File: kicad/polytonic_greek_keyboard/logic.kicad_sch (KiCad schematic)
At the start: 1 part, among them U1 ESP32-S2-WROVER

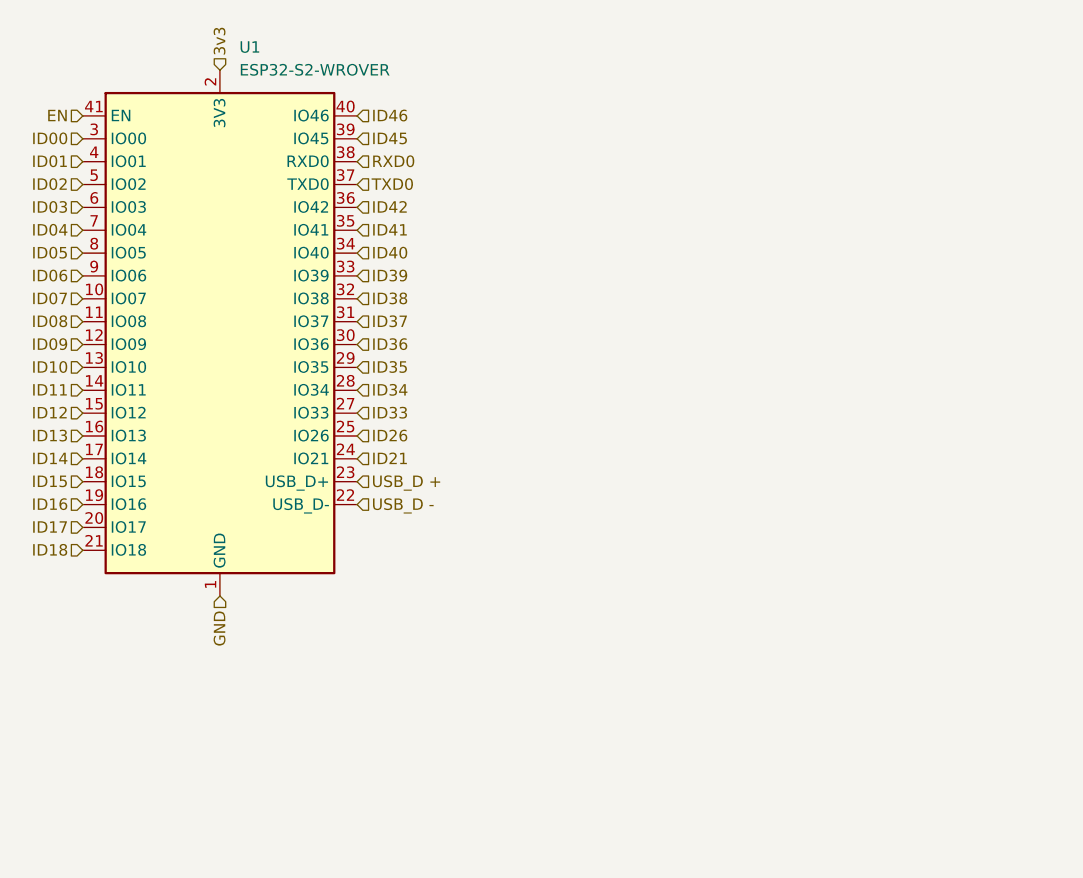
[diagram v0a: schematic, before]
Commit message: [UPDATE] the board desing, [FIX] connection issues
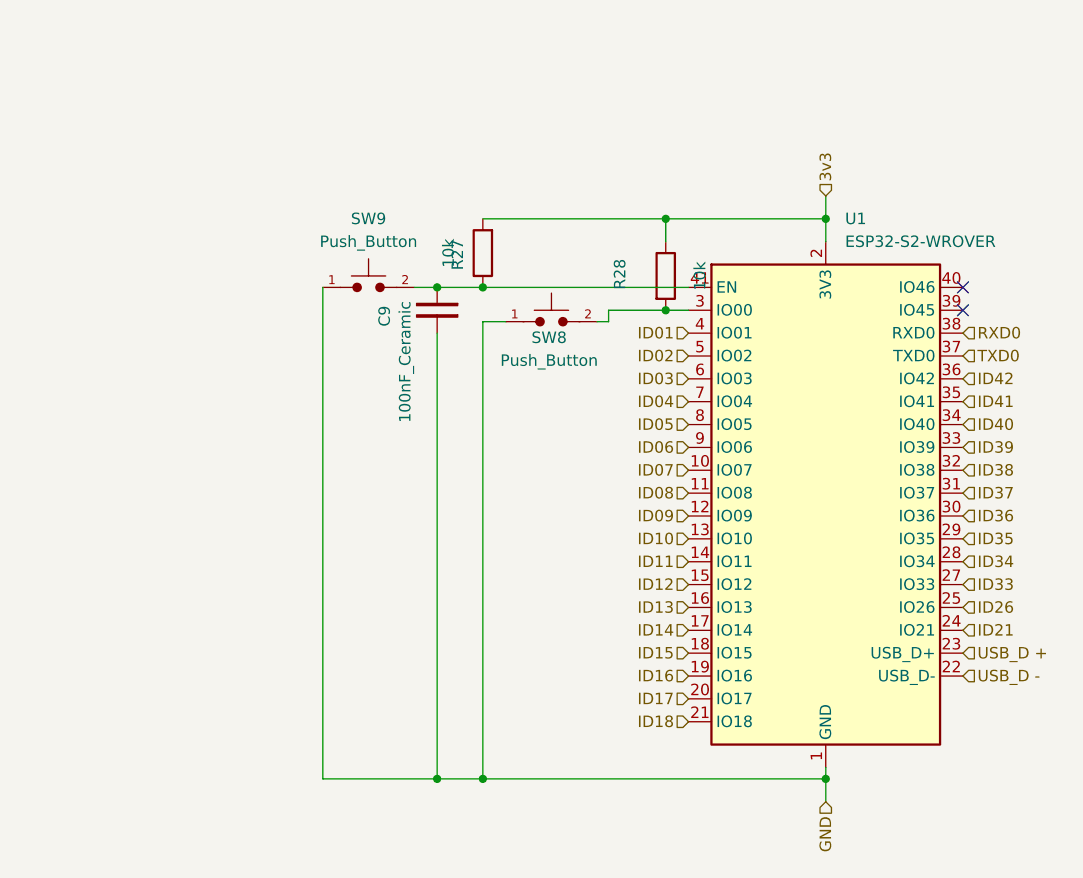
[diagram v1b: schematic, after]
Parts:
- added C9: 100nF_Ceramic, Capacitor_THT:C_Disc_D5.0mm_W2.5mm_P2.50mm, symbol PCM_SL_Capacitors:100nF_Ceramic
- added R27, R28: 10k_0402, Resistor_SMD:R_0402_1005Metric, symbol PCM_4ms_Resistor:10k_0402
- added SW8, SW9: Push_Button, Button_Switch_THT:SW_PUSH_6mm, symbol PCM_SL_Devices:Push_Button
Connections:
- net 3v3: now also R27.2, R28.1
- net GND: now also C9.2, SW8.1, SW9.1
- net EN: no longer names the net of U1.41 (EN)
- net EN: now also C9.1, R27.1, SW9.2
- net ID00: no longer names the net of U1.3 (IO00)
- net ID00: now also R28.2, SW8.2
- net ID45: no longer names the net of U1.39 (IO45)
- net ID46: no longer names the net of U1.40 (IO46)
- no-connect marks 0 -> 2
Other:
- moved on the sheet: U1

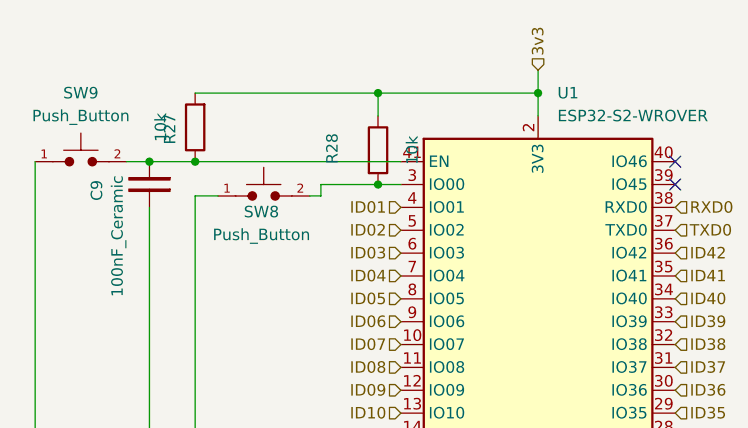
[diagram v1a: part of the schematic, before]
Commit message: [UPDATE] the desing to fit on two separate pcbs
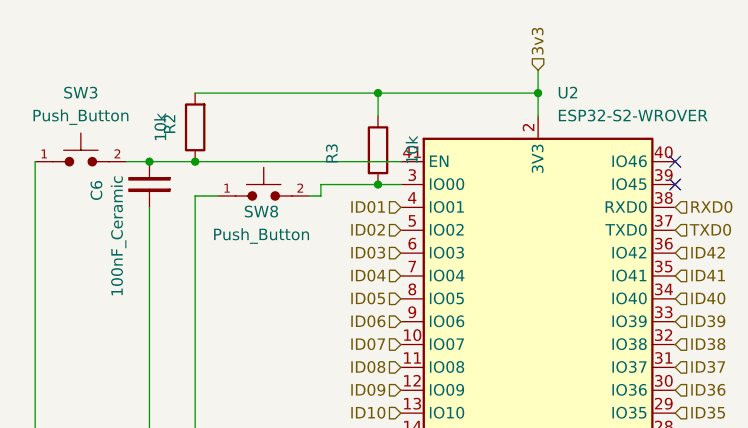
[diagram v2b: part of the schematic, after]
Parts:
- renumbered C9 to C6, R27 to R2, R28 to R3, SW9 to SW3, U1 to U2
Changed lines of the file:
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@@
 		(on_board yes)
 		(dnp no)
-		(property "Reference" "R28"
+		(property "Reference" "R3"
 			(at 90.17 47.244 90)
 			(effects
@@
 		(instances
 			(project "polytonic_greek_keyboard"
-				(path "/cbe25a1b-6c02-43c2-9ff9-ba274c7cf6a2/98a216ce-7319-4f0b-a321-c8ded0ff5837"
-					(reference "R28")
+				(path "/cbe25a1b-6c02-43c2-9ff9-ba274c7cf6a2/8498b325-11fd-4b20-a704-75ec3d8987ef/52990bdd-0b84-441a-b927-02579db6fb17"
+					(reference "R3")
 					(unit 1)
 				)
@@
 		(dnp no)
 		(fields_autoplaced yes)
-		(property "Reference" "U1"
+		(property "Reference" "U2"
 			(at 115.1733 39.37 0)
 			(effects
@@
 		)
 		(instances
-			(project ""
-				(path "/cbe25a1b-6c02-43c2-9ff9-ba274c7cf6a2/98a216ce-7319-4f0b-a321-c8ded0ff5837"
-					(reference "U1")
+			(project "polytonic_greek_keyboard"
+				(path "/cbe25a1b-6c02-43c2-9ff9-ba274c7cf6a2/8498b325-11fd-4b20-a704-75ec3d8987ef/52990bdd-0b84-441a-b927-02579db6fb17"
+					(reference "U2")
 					(unit 1)
 				)
@@
 		(on_board yes)
 		(dnp no)
-		(property "Reference" "C9"
+		(property "Reference" "C6"
 			(at 64.008 49.022 0)
 			(effects
@@
 		)
 		(instances
-			(project ""
-				(path "/cbe25a1b-6c02-43c2-9ff9-ba274c7cf6a2/98a216ce-7319-4f0b-a321-c8ded0ff5837"
-					(reference "C9")
+			(project "polytonic_greek_keyboard"
+				(path "/cbe25a1b-6c02-43c2-9ff9-ba274c7cf6a2/8498b325-11fd-4b20-a704-75ec3d8987ef/52990bdd-0b84-441a-b927-02579db6fb17"
+					(reference "C6")
 					(unit 1)
 				)
@@
 		(dnp no)
 		(fields_autoplaced yes)
-		(property "Reference" "SW9"
+		(property "Reference" "SW3"
 			(at 62.23 39.37 0)
 			(effects
@@
 		)
 		(instances
-			(project ""
-				(path "/cbe25a1b-6c02-43c2-9ff9-ba274c7cf6a2/98a216ce-7319-4f0b-a321-c8ded0ff5837"
-					(reference "SW9")
+			(project "polytonic_greek_keyboard"
+				(path "/cbe25a1b-6c02-43c2-9ff9-ba274c7cf6a2/8498b325-11fd-4b20-a704-75ec3d8987ef/52990bdd-0b84-441a-b927-02579db6fb17"
+					(reference "SW3")
 					(unit 1)
 				)
@@
 		(on_board yes)
 		(dnp no)
-		(property "Reference" "R27"
+		(property "Reference" "R2"
 			(at 72.136 41.656 90)
 			(effects
@@
 		)
 		(instances
-			(project ""
-				(path "/cbe25a1b-6c02-43c2-9ff9-ba274c7cf6a2/98a216ce-7319-4f0b-a321-c8ded0ff5837"
-					(reference "R27")
+			(project "polytonic_greek_keyboard"
+				(path "/cbe25a1b-6c02-43c2-9ff9-ba274c7cf6a2/8498b325-11fd-4b20-a704-75ec3d8987ef/52990bdd-0b84-441a-b927-02579db6fb17"
+					(reference "R2")
 					(unit 1)
 				)
@@
 		(instances
 			(project "polytonic_greek_keyboard"
-				(path "/cbe25a1b-6c02-43c2-9ff9-ba274c7cf6a2/98a216ce-7319-4f0b-a321-c8ded0ff5837"
+				(path "/cbe25a1b-6c02-43c2-9ff9-ba274c7cf6a2/8498b325-11fd-4b20-a704-75ec3d8987ef/52990bdd-0b84-441a-b927-02579db6fb17"
 					(reference "SW8")
 					(unit 1)

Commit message: [UPDATE] anotation issues
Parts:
- renumbered C6 to C4, R3 to R10, R2 to R9, SW8 to SW4, U2 to U3
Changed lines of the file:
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@@
 		(on_board yes)
 		(dnp no)
-		(property "Reference" "R3"
+		(property "Reference" "R10"
 			(at 90.17 47.244 90)
 			(effects
@@
 			(project "polytonic_greek_keyboard"
 				(path "/cbe25a1b-6c02-43c2-9ff9-ba274c7cf6a2/8498b325-11fd-4b20-a704-75ec3d8987ef/52990bdd-0b84-441a-b927-02579db6fb17"
-					(reference "R3")
+					(reference "R10")
 					(unit 1)
 				)
@@
 		(dnp no)
 		(fields_autoplaced yes)
-		(property "Reference" "U2"
+		(property "Reference" "U3"
 			(at 115.1733 39.37 0)
 			(effects
@@
 			(project "polytonic_greek_keyboard"
 				(path "/cbe25a1b-6c02-43c2-9ff9-ba274c7cf6a2/8498b325-11fd-4b20-a704-75ec3d8987ef/52990bdd-0b84-441a-b927-02579db6fb17"
-					(reference "U2")
+					(reference "U3")
 					(unit 1)
 				)
@@
 		(on_board yes)
 		(dnp no)
-		(property "Reference" "C6"
+		(property "Reference" "C4"
 			(at 64.008 49.022 0)
 			(effects
@@
 			(project "polytonic_greek_keyboard"
 				(path "/cbe25a1b-6c02-43c2-9ff9-ba274c7cf6a2/8498b325-11fd-4b20-a704-75ec3d8987ef/52990bdd-0b84-441a-b927-02579db6fb17"
-					(reference "C6")
+					(reference "C4")
 					(unit 1)
 				)
@@
 		(on_board yes)
 		(dnp no)
-		(property "Reference" "R2"
+		(property "Reference" "R9"
 			(at 72.136 41.656 90)
 			(effects
@@
 			(project "polytonic_greek_keyboard"
 				(path "/cbe25a1b-6c02-43c2-9ff9-ba274c7cf6a2/8498b325-11fd-4b20-a704-75ec3d8987ef/52990bdd-0b84-441a-b927-02579db6fb17"
-					(reference "R2")
+					(reference "R9")
 					(unit 1)
 				)
@@
 		(on_board yes)
 		(dnp no)
-		(property "Reference" "SW8"
+		(property "Reference" "SW4"
 			(at 82.296 52.578 0)
 			(effects
@@
 			(project "polytonic_greek_keyboard"
 				(path "/cbe25a1b-6c02-43c2-9ff9-ba274c7cf6a2/8498b325-11fd-4b20-a704-75ec3d8987ef/52990bdd-0b84-441a-b927-02579db6fb17"
-					(reference "SW8")
+					(reference "SW4")
 					(unit 1)
 				)

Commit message: [UPDATE] the final merged version of the schematic before splitting into two separate kicad projects
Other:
- company: (none) -> Henry's Software House
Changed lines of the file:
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@@
 	(generator_version "9.0")
 	(paper "A4")
+	(title_block
+		(rev "1 - do not edit connector pin layout.")
+		(company "Henry's Software House")
+	)
 	(junction
 		(at 74.93 46.99)
